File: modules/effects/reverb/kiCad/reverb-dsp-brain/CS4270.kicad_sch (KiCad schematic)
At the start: 16 parts, among them U2 CS4270

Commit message: finished clouds clone (weathering/the storm)
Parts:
- added C12, C20: 100nF, Capacitor_SMD:C_0805_2012Metric_Pad1.18x1.45mm_HandSolder, symbol Device:C
- added C19: 10uF, Capacitor_SMD:C_0805_2012Metric_Pad1.18x1.45mm_HandSolder, symbol Device:C
- C10, C11, C13, C14, C15, C16, C17, C18: footprint (none) -> Capacitor_SMD:C_0805_2012Metric_Pad1.18x1.45mm_HandSolder
- R10, R3, R4, R6, R7, R8, R9: footprint (none) -> Resistor_SMD:R_0805_2012Metric_Pad1.20x1.40mm_HandSolder
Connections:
- net +3.3V: now also R6.1, C12.1, C19.1, C20.1
- net GNDREF: now also C12.2, C19.2, C20.2; no longer R6.1
- net +3.3VA renamed +5VA
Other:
- note removed: "Seems like VA should be 5V?"
- moved on the sheet: C15, C16, R6

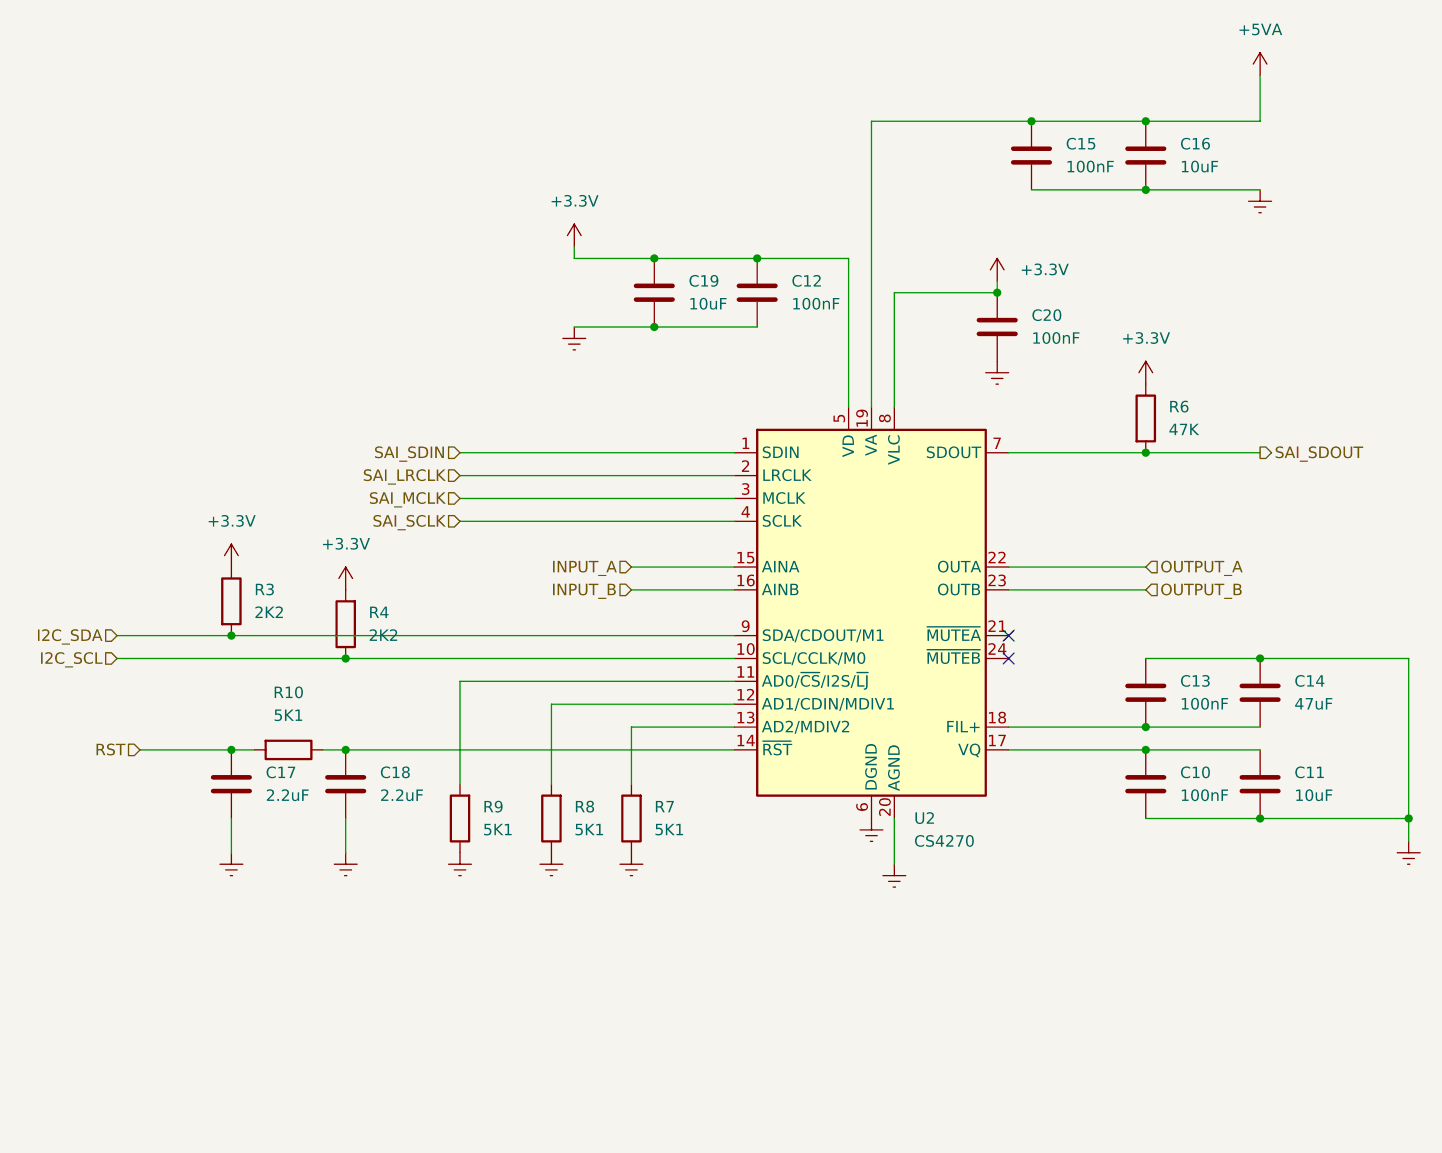
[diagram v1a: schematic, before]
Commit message: Setup of C code for Reverb
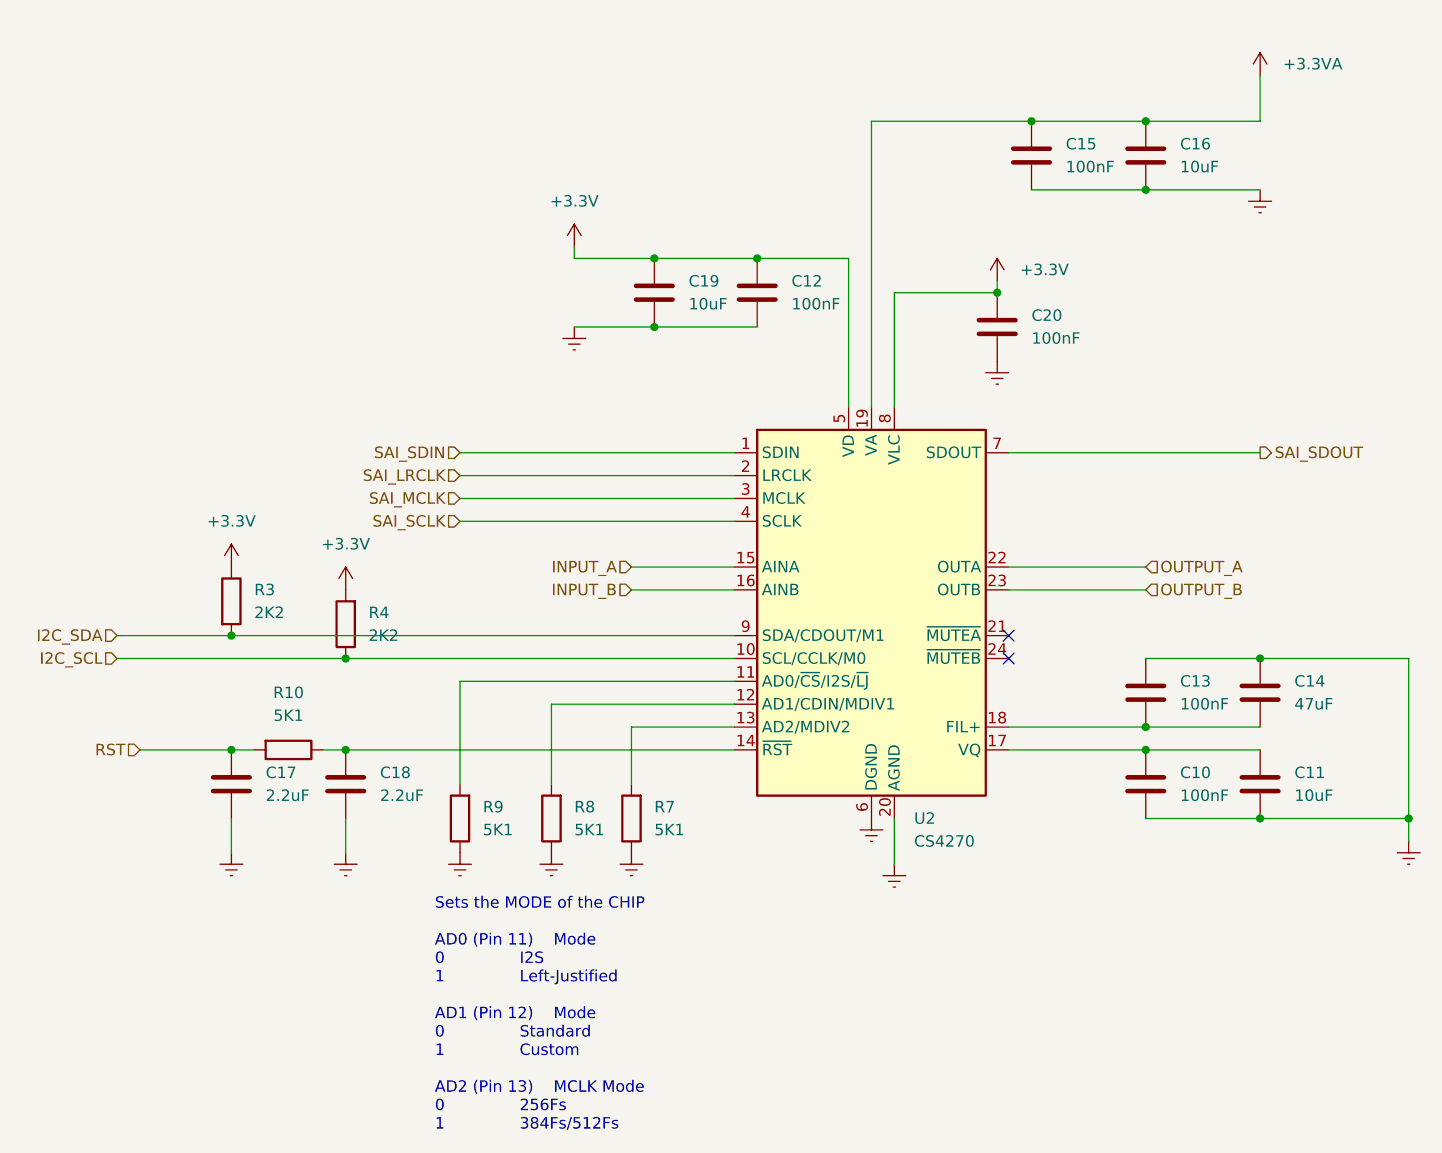
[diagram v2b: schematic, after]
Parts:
- removed R6: 47K, Resistor_SMD:R_0805_2012Metric_Pad1.20x1.40mm_HandSolder, symbol Device:R
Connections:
- net +5VA renamed +3.3VA
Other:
- note added: "Sets the MODE of the CHIP AD0 (Pin 11) Mode 0 I2S 1 Left-Justified AD1 (Pin 12) Mode 0 Standard 1 Custom AD2 (Pin 13) MCLK Mode 0 256Fs 1 384Fs/512Fs"
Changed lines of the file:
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@@
 	(paper "A4")
-	(junction
-		(at 165.1 71.12)
-		(diameter 0)
-		(color 0 0 0 0)
-	)
 	(junction
 		(at 165.1 104.14)
@@
 	(wire
 		(pts
-			(xy 149.86 71.12) (xy 165.1 71.12)
+			(xy 149.86 71.12) (xy 177.8 71.12)
 		)
 		(stroke
@@
 	(wire
 		(pts
-			(xy 165.1 71.12) (xy 177.8 71.12)
-		)
-		(stroke
-			(width 0)
-			(type default)
-		)
-	)
-	(wire
-		(pts
 			(xy 88.9 96.52) (xy 88.9 107.95)
 		)
@@
 			(width 0)
 			(type default)
+		)
+	)
+	(text "Sets the MODE of the CHIP\n\nAD0 (Pin 11)    Mode\n0               I2S\n1               Left-Justified\n\nAD1 (Pin 12)    Mode\n0               Standard\n1               Custom\n\nAD2 (Pin 13)    MCLK Mode\n0               256Fs\n1               384Fs/512Fs"
+		(exclude_from_sim no)
+		(at 86.106 133.604 0)
+		(effects
+			(font
+				(size 1.27 1.27)
+			)
+			(justify left)
 		)
 	)
@@
 	)
 	(symbol
-		(lib_id "power:+3.3V")
-		(at 165.1 63.5 0)
-		(unit 1)
-		(exclude_from_sim no)
-		(in_bom yes)
-		(on_board yes)
-		(dnp no)
-		(fields_autoplaced yes)
-		(property "Reference" "#PWR039"
-			(at 165.1 67.31 0)
-			(effects
-				(font
-					(size 1.27 1.27)
-				)
-				(hide yes)
-			)
-		)
-		(property "Value" "+3.3V"
-			(at 165.1 58.42 0)
-			(effects
-				(font
-					(size 1.27 1.27)
-				)
-			)
-		)
-		(property "Footprint" ""
-			(at 165.1 63.5 0)
-			(effects
-				(font
-					(size 1.27 1.27)
-				)
-				(hide yes)
-			)
-		)
-		(property "Datasheet" ""
-			(at 165.1 63.5 0)
-			(effects
-				(font
-					(size 1.27 1.27)
-				)
-				(hide yes)
-			)
-		)
-		(property "Description" "Power symbol creates a global label with name \"+3.3V\""
-			(at 165.1 63.5 0)
-			(effects
-				(font
-					(size 1.27 1.27)
-				)
-				(hide yes)
-			)
-		)
-		(pin "1"
-		)
-		(instances
-			(project "reverb-dsp-brain"
-				(path "/d434ae79-d86c-4782-b5e7-77d1f29745ae/d5cbbb62-576c-47e8-bd32-3ebbeaee0e2b"
-					(reference "#PWR039")
-					(unit 1)
-				)
-			)
-		)
-	)
-	(symbol
 		(lib_id "Device:C")
 		(at 177.8 107.95 0)
@@
 	)
 	(symbol
+		(lib_id "power:+3.3V")
+		(at 177.8 29.21 0)
+		(unit 1)
+		(exclude_from_sim no)
+		(in_bom yes)
+		(on_board yes)
+		(dnp no)
+		(fields_autoplaced yes)
+		(property "Reference" "#PWR017"
+			(at 177.8 33.02 0)
+			(effects
+				(font
+					(size 1.27 1.27)
+				)
+				(hide yes)
+			)
+		)
+		(property "Value" "+3.3VA"
+			(at 180.34 27.9399 0)
+			(effects
+				(font
+					(size 1.27 1.27)
+				)
+				(justify left)
+			)
+		)
+		(property "Footprint" ""
+			(at 177.8 29.21 0)
+			(effects
+				(font
+					(size 1.27 1.27)
+				)
+				(hide yes)
+			)
+		)
+		(property "Datasheet" ""
+			(at 177.8 29.21 0)
+			(effects
+				(font
+					(size 1.27 1.27)
+				)
+				(hide yes)
+			)
+		)
+		(property "Description" "Power symbol creates a global label with name \"+3.3V\""
+			(at 177.8 29.21 0)
+			(effects
+				(font
+					(size 1.27 1.27)
+				)
+				(hide yes)
+			)
+		)
+		(pin "1"
+		)
+		(instances
+			(project "reverb-dsp-brain"
+				(path "/d434ae79-d86c-4782-b5e7-77d1f29745ae/d5cbbb62-576c-47e8-bd32-3ebbeaee0e2b"
+					(reference "#PWR017")
+					(unit 1)
+				)
+			)
+		)
+	)
+	(symbol
 		(lib_id "Audio:CS4270")
 		(at 134.62 88.9 0)
@@
 	)
 	(symbol
-		(lib_id "power:+5VA")
-		(at 177.8 29.21 0)
-		(unit 1)
-		(exclude_from_sim no)
-		(in_bom yes)
-		(on_board yes)
-		(dnp no)
-		(fields_autoplaced yes)
-		(property "Reference" "#PWR031"
-			(at 177.8 33.02 0)
-			(effects
-				(font
-					(size 1.27 1.27)
-				)
-				(hide yes)
-			)
-		)
-		(property "Value" "+5VA"
-			(at 177.8 24.13 0)
-			(effects
-				(font
-					(size 1.27 1.27)
-				)
-			)
-		)
-		(property "Footprint" ""
-			(at 177.8 29.21 0)
-			(effects
-				(font
-					(size 1.27 1.27)
-				)
-				(hide yes)
-			)
-		)
-		(property "Datasheet" ""
-			(at 177.8 29.21 0)
-			(effects
-				(font
-					(size 1.27 1.27)
-				)
-				(hide yes)
-			)
-		)
-		(property "Description" "Power symbol creates a global label with name \"+5VA\""
-			(at 177.8 29.21 0)
-			(effects
-				(font
-					(size 1.27 1.27)
-				)
-				(hide yes)
-			)
-		)
-		(pin "1"
-		)
-		(instances
-			(project ""
-				(path "/d434ae79-d86c-4782-b5e7-77d1f29745ae/d5cbbb62-576c-47e8-bd32-3ebbeaee0e2b"
-					(reference "#PWR031")
-					(unit 1)
-				)
-			)
-		)
-	)
-	(symbol
 		(lib_id "Device:R")
 		(at 63.5 87.63 0)
@@
 					(unit 1)
 				)
-			)
-		)
-	)
-	(symbol
-		(lib_id "Device:R")
-		(at 165.1 67.31 0)
-		(unit 1)
-		(exclude_from_sim no)
-		(in_bom yes)
-		(on_board yes)
-		(dnp no)
-		(fields_autoplaced yes)
-		(property "Reference" "R6"
-			(at 167.64 66.0399 0)
-			(effects
-				(font
-					(size 1.27 1.27)
-				)
-				(justify left)
-			)
-		)
-		(property "Value" "47K"
-			(at 167.64 68.5799 0)
-			(effects
-				(font
-					(size 1.27 1.27)
-				)
-				(justify left)
-			)
-		)
-		(property "Footprint" "Resistor_SMD:R_0805_2012Metric_Pad1.20x1.40mm_HandSolder"
-			(at 163.322 67.31 90)
-			(effects
-				(font
-					(size 1.27 1.27)
-				)
-				(hide yes)
-			)
-		)
-		(property "Datasheet" "~"
-			(at 165.1 67.31 0)
-			(effects
-				(font
-					(size 1.27 1.27)
-				)
-				(hide yes)
-			)
-		)
-		(property "Description" "Resistor"
-			(at 165.1 67.31 0)
-			(effects
-				(font
-					(size 1.27 1.27)
-				)
-				(hide yes)
-			)
-		)
-		(pin "2"
-		)
-		(pin "1"
-		)
-		(instances
-			(project "reverb-dsp-brain"
-				(path "/d434ae79-d86c-4782-b5e7-77d1f29745ae/d5cbbb62-576c-47e8-bd32-3ebbeaee0e2b"
-					(reference "R6")
-					(unit 1)
-				)
